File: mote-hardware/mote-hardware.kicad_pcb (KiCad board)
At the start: 2 copper layers, 93.6 x 102.8 mm, 67 parts, among them J1 USB_C_Receptacle_USB2.0_14P, J2 JST_XH2.54-SP, J4 SM03B-SRSS-TB, J5 Conn_01x03_Pin, J6 Conn_01x03_Pin, J7 JST_PH_B6B, J8 JST_PH_B6B, SW1 SW_Push, SW2 SW_Push, U1 RP2354_60QFN, U2 NCP1117-3.3_SOT223, U4 RP Radio Module 2, U5 DRV8833PW, U9 LSM6DS3, Y1 ABM8-272-T3

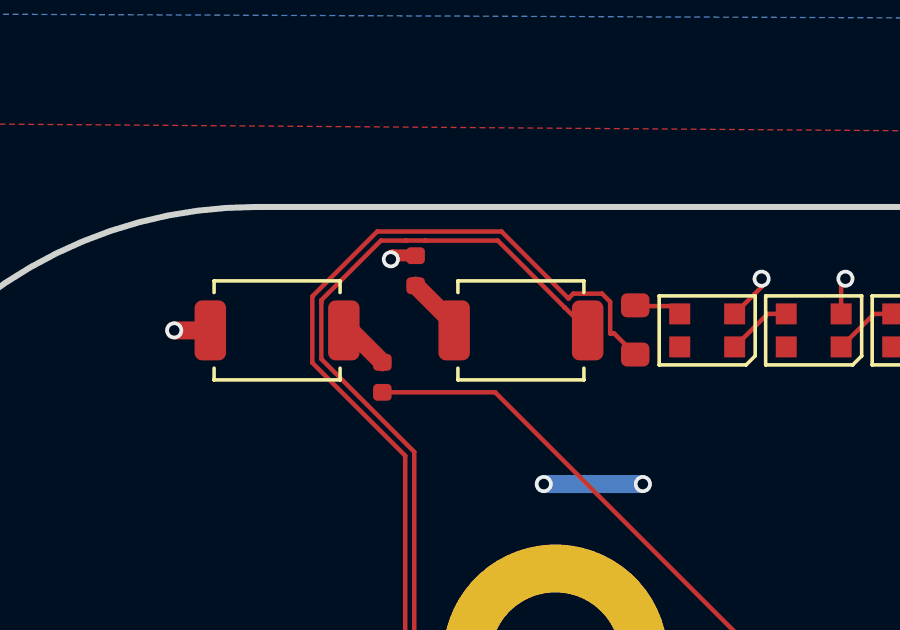
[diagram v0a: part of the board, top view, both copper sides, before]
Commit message: Add 3d models
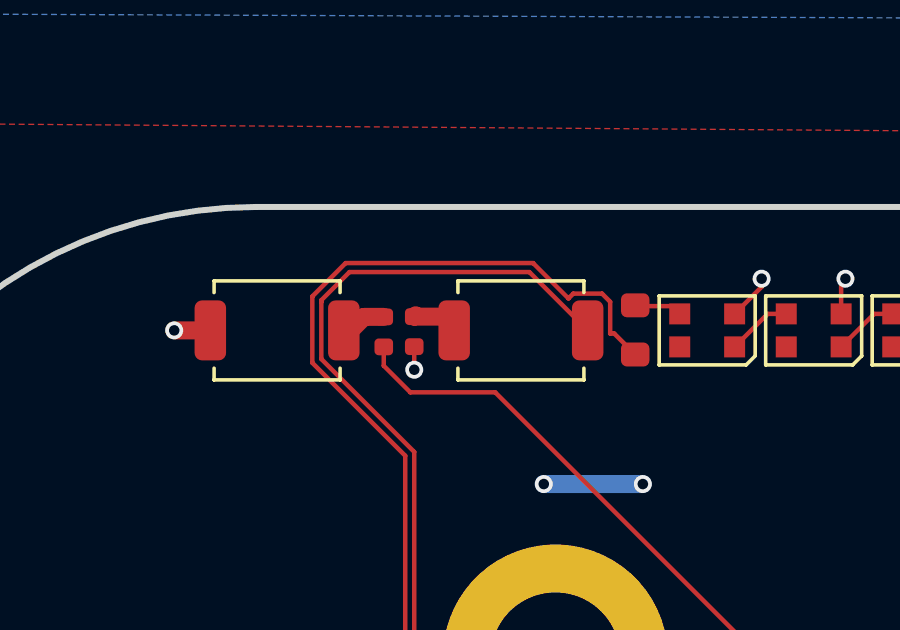
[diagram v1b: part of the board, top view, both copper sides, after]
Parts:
- moved R4 2.03 mm to (72.9, 43.7), turned to -90 degrees
- moved R6 1.51 mm to (71.9, 43.7)
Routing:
- net /rp2354/QSPI_SS: track 57.2 -> 58.1 mm
- net /status_led_tx: track 140.1 -> 139.2 mm
- net /rp2354/RUN: track 132.2 -> 131.4 mm

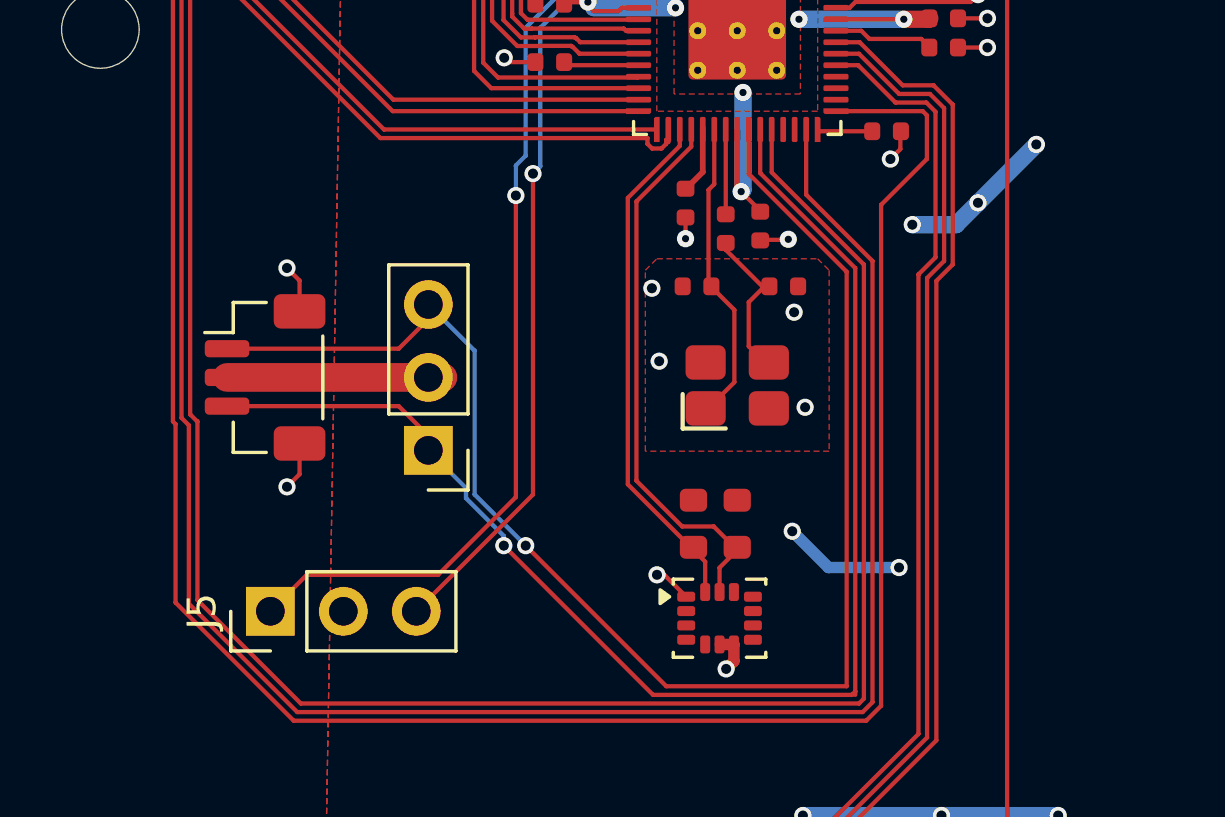
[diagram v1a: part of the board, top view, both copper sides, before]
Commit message: Add comments to schematic, respect ground pin on SWD and UART connectors
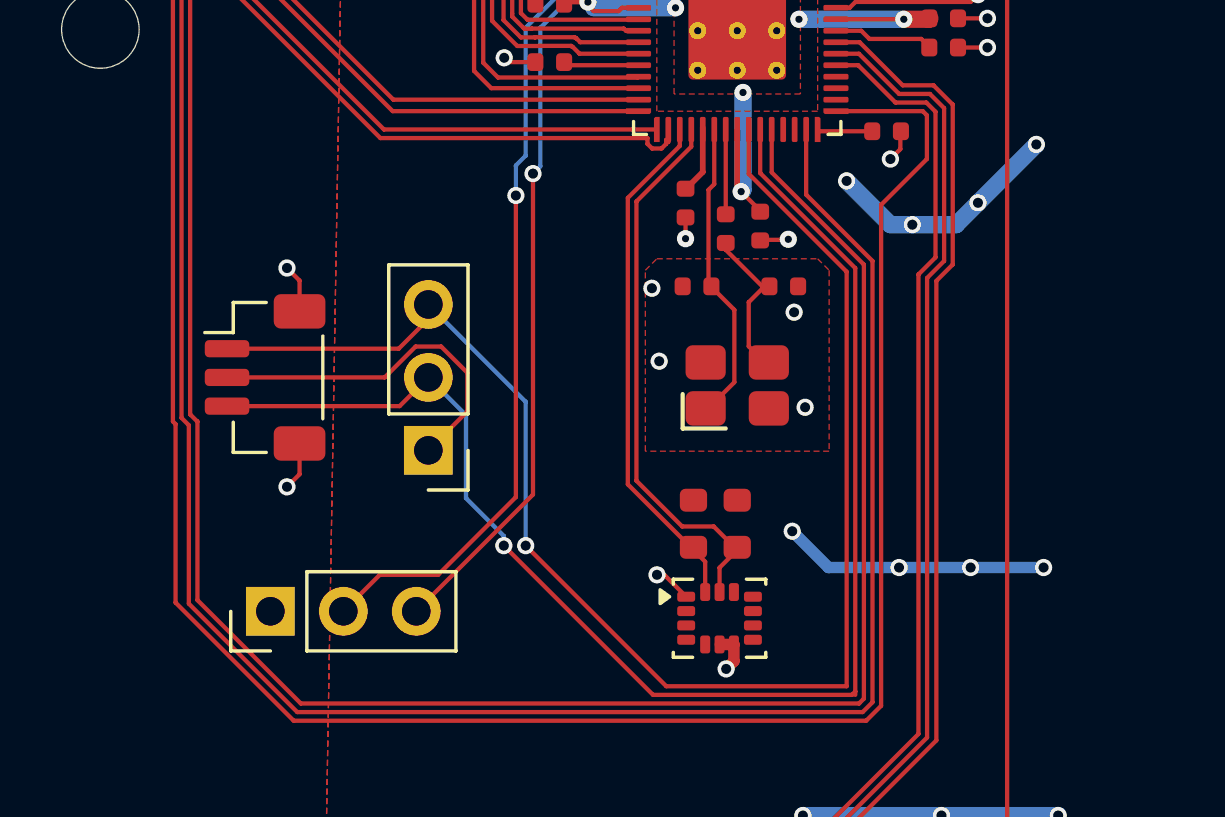
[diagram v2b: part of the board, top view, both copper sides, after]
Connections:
- J5 pad 1: /rp2354/UART0_TX -> GND
- J5 pad 2: GND -> /rp2354/UART0_TX
- J6 pad 1: /rp2354/SWD -> GND
- J6 pad 2: GND -> /rp2354/SWD
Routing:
- net /+3v3: track 67.2 -> 75.2 mm, vias 11 -> 14
- net GND: track 77.9 -> 82.9 mm
- net /rp2354/UART0_TX: track 32.0 -> 29.4 mm
- net /rp2354/SWD: track 48.1 -> 49.9 mm
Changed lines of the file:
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@@
 			(layers "*.Cu" "*.Mask")
 			(remove_unused_layers no)
-			(net 26 "/rp2354/SWD")
+			(net 1 "GND")
 			(pinfunction "Pin_1")
 			(pintype "passive")
@@
 			(layers "*.Cu" "*.Mask")
 			(remove_unused_layers no)
-			(net 1 "GND")
+			(net 26 "/rp2354/SWD")
 			(pinfunction "Pin_2")
 			(pintype "passive")
@@
 		)
 		(property "Value" "10u"
-			(at 0 1.68 0)
+			(at 0.254 -1.778 0)
 			(layer "F.Fab")
 			(effects
@@
 		)
 		(property "Value" "WS2812B-2020"
-			(at 0 2.2 0)
+			(at -2.935 2.752 0)
 			(layer "F.Fab")
 			(effects
@@
 		)
 		(property "Value" "WS2812B-2020"
-			(at 0 2.2 0)
+			(at 4.165 2.752 0)
 			(layer "F.Fab")
 			(effects
@@
 		)
 		(property "Value" "WS2812B-2020"
-			(at 0 2.2 0)
+			(at 0.615 2.752 0)
 			(layer "F.Fab")
 			(effects
@@
 		(property "Reference" "J5"
 			(at 0 -2.38 90)
-			(layer "F.SilkS")
+			(layer "Dwgs.User")
 			(effects
 				(font
@@
 			(layers "*.Cu" "*.Mask")
 			(remove_unused_layers no)
-			(net 70 "/rp2354/UART0_TX")
+			(net 1 "GND")
 			(pinfunction "Pin_1")
 			(pintype "passive")
@@
 			(layers "*.Cu" "*.Mask")
 			(remove_unused_layers no)
-			(net 1 "GND")
+			(net 70 "/rp2354/UART0_TX")
 			(pinfunction "Pin_2")
 			(pintype "passive")
@@
 	)
 	(segment
-		(start 83.582 72.1021)
-		(end 83.582001 72.102099)
-		(width 0.4)
+		(start 90.678 104.97672)
+		(end 90.678 106.323)
+		(width 0.15)
 		(layer "F.Cu")
 		(net 1)
 	)
 	(segment
-		(start 82.311 105.14)
-		(end 89.829 105.14)
-		(width 1)
+		(start 83.582 72.1021)
+		(end 83.582001 72.102099)
+		(width 0.4)
 		(layer "F.Cu")
 		(net 1)
@@
 	)
 	(segment
+		(start 87.80072 105.14)
+		(end 88.87572 104.065)
+		(width 0.15)
+		(layer "F.Cu")
+		(net 1)
+	)
+	(segment
 		(start 98.298 112.776)
 		(end 97.536 112.014)
@@
 	)
 	(segment
+		(start 82.311 105.14)
+		(end 87.80072 105.14)
+		(width 0.15)
+		(layer "F.Cu")
+		(net 1)
+	)
+	(segment
 		(start 87.128 43.096)
 		(end 87.128 42.066)
@@
 	)
 	(segment
+		(start 89.76628 104.065)
+		(end 90.678 104.97672)
+		(width 0.15)
+		(layer "F.Cu")
+		(net 1)
+	)
+	(segment
 		(start 84.598 76.496)
 		(end 84.556 76.454)
@@
 	)
 	(segment
+		(start 90.678 106.323)
+		(end 89.321 107.68)
+		(width 0.15)
+		(layer "F.Cu")
+		(net 1)
+	)
+	(segment
 		(start 83.578 43.096)
 		(end 84.477 42.197)
@@
 	)
 	(segment
+		(start 88.87572 104.065)
+		(end 89.76628 104.065)
+		(width 0.15)
+		(layer "F.Cu")
+		(net 1)
+	)
+	(segment
 		(start 113.552 51.322)
 		(end 113.538 51.308)
@@
 	)
 	(via
+		(at 108.204 111.76)
+		(size 0.6)
+		(drill 0.35)
+		(layers "F.Cu" "B.Cu")
+		(net 10)
+	)
+	(via
 		(at 101.991029 110.496075)
 		(size 0.6)
@@
 	)
 	(via
+		(at 103.886 98.298)
+		(size 0.6)
+		(drill 0.35)
+		(layers "F.Cu" "B.Cu")
+		(net 10)
+	)
+	(via
 		(at 94.996 88.392)
 		(size 0.6)
@@
 	)
 	(via
+		(at 110.744 111.76)
+		(size 0.6)
+		(drill 0.35)
+		(layers "F.Cu" "B.Cu")
+		(net 10)
+	)
+	(via
 		(at 111.252 120.396)
 		(size 0.6)
@@
 	)
 	(segment
+		(start 108.204 111.76)
+		(end 110.744 111.76)
+		(width 0.4)
+		(layer "B.Cu")
+		(net 10)
+	)
+	(segment
 		(start 107.188 120.396)
 		(end 111.252 120.396)
@@
 	)
 	(segment
+		(start 105.41 99.822)
+		(end 103.886 98.298)
+		(width 0.6)
+		(layer "B.Cu")
+		(net 10)
+	)
+	(segment
 		(start 88.138 68.7945)
 		(end 88.234 68.8905)
@@
 	)
 	(segment
+		(start 105.711 111.76)
+		(end 108.204 111.76)
+		(width 0.4)
+		(layer "B.Cu")
+		(net 10)
+	)
+	(segment
 		(start 102.362 120.396)
 		(end 107.188 120.396)
@@
 	)
 	(segment
+		(start 106.172 99.822)
+		(end 105.41 99.822)
+		(width 0.6)
+		(layer "B.Cu")
+		(net 10)
+	)
+	(segment
 		(start 101.276 89.134)
 		(end 101.08 88.938)
@@
 	(segment
 		(start 92.71 110.998)
-		(end 90.932 109.22)
+		(end 92.71 105.989)
 		(width 0.15)
 		(layer "B.Cu")
@@
 	)
 	(segment
-		(start 90.932 109.22)
-		(end 90.932 104.211)
-		(width 0.15)
-		(layer "B.Cu")
-		(net 25)
-	)
-	(segment
-		(start 90.932 104.211)
+		(start 92.71 105.989)
 		(end 89.321 102.6)
 		(width 0.15)
@@
 	)
 	(segment
-		(start 88.289 106.14)
-		(end 89.829 107.68)
-		(width 0.15)
-		(layer "F.Cu")
-		(net 26)
-	)
-	(segment
 		(start 82.311 106.14)
-		(end 88.289 106.14)
+		(end 88.321 106.14)
 		(width 0.15)
 		(layer "F.Cu")
@@
 	)
 	(segment
+		(start 88.321 106.14)
+		(end 89.321 105.14)
+		(width 0.15)
+		(layer "F.Cu")
+		(net 26)
+	)
+	(segment
 		(start 104.186 116.078)
 		(end 104.186 116.194)
@@
 	)
 	(segment
-		(start 90.632 108.991)
-		(end 89.321 107.68)
+		(start 90.632 109.344264)
+		(end 90.632 106.451)
 		(width 0.15)
 		(layer "B.Cu")
@@
 	)
 	(segment
-		(start 91.948 110.998)
-		(end 91.948 110.660264)
+		(start 90.632 106.451)
+		(end 89.321 105.14)
 		(width 0.15)
 		(layer "B.Cu")
@@
 	)
 	(segment
-		(start 90.632 109.344264)
-		(end 90.632 108.991)
+		(start 91.948 110.660264)
+		(end 90.632 109.344264)
 		(width 0.15)
 		(layer "B.Cu")
@@
 	)
 	(segment
-		(start 91.948 110.660264)
-		(end 90.632 109.344264)
+		(start 91.948 110.998)
+		(end 91.948 110.660264)
 		(width 0.15)
 		(layer "B.Cu")
@@
 	)
 	(segment
-		(start 85.09 112.014)
-		(end 89.662 112.014)
+		(start 89.662 112.014)
+		(end 87.63 112.014)
 		(width 0.15)
 		(layer "F.Cu")
@@
 	)
 	(segment
-		(start 89.662 112.014)
-		(end 92.367997 109.308003)
+		(start 87.63 112.014)
+		(end 86.36 113.284)
 		(width 0.15)
 		(layer "F.Cu")
@@
 	)
 	(segment
-		(start 83.82 113.284)
-		(end 85.09 112.014)
+		(start 89.662 112.014)
+		(end 92.367997 109.308003)
 		(width 0.15)
 		(layer "F.Cu")

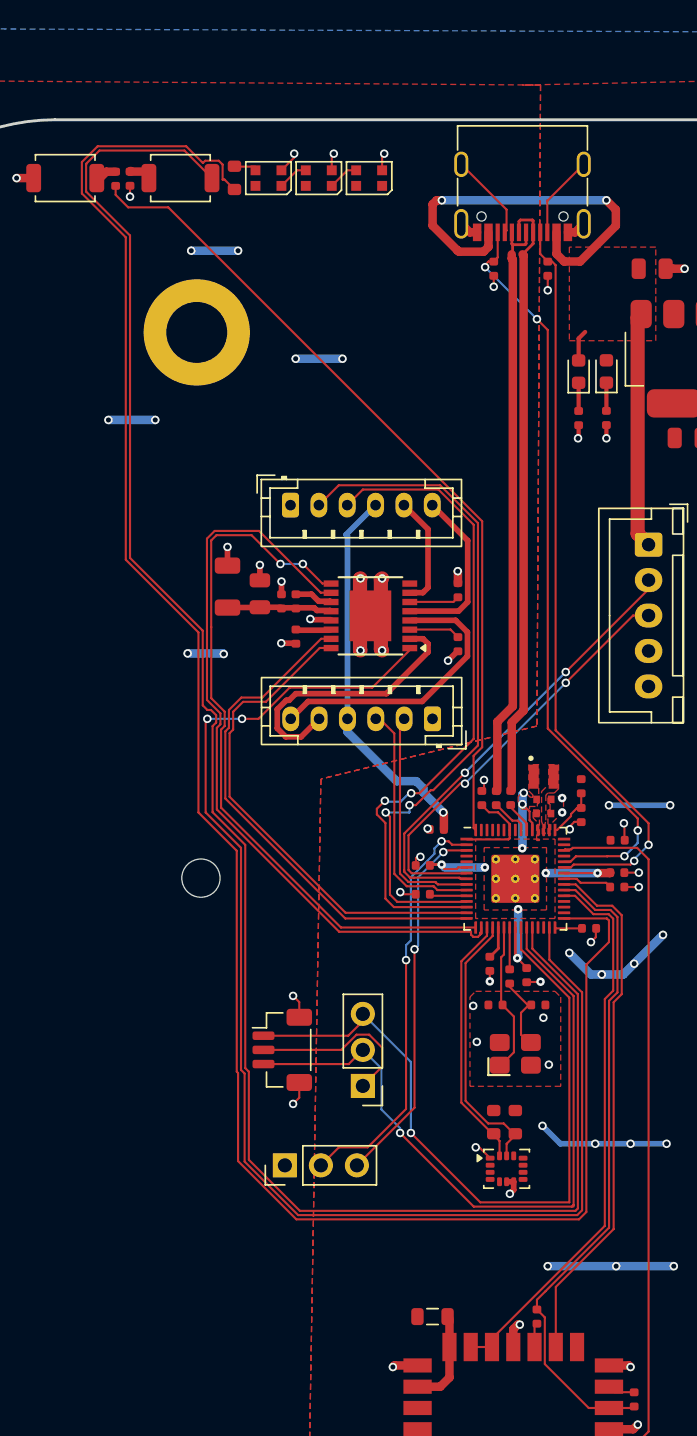
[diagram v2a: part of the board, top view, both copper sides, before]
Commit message: reformated a couple traces
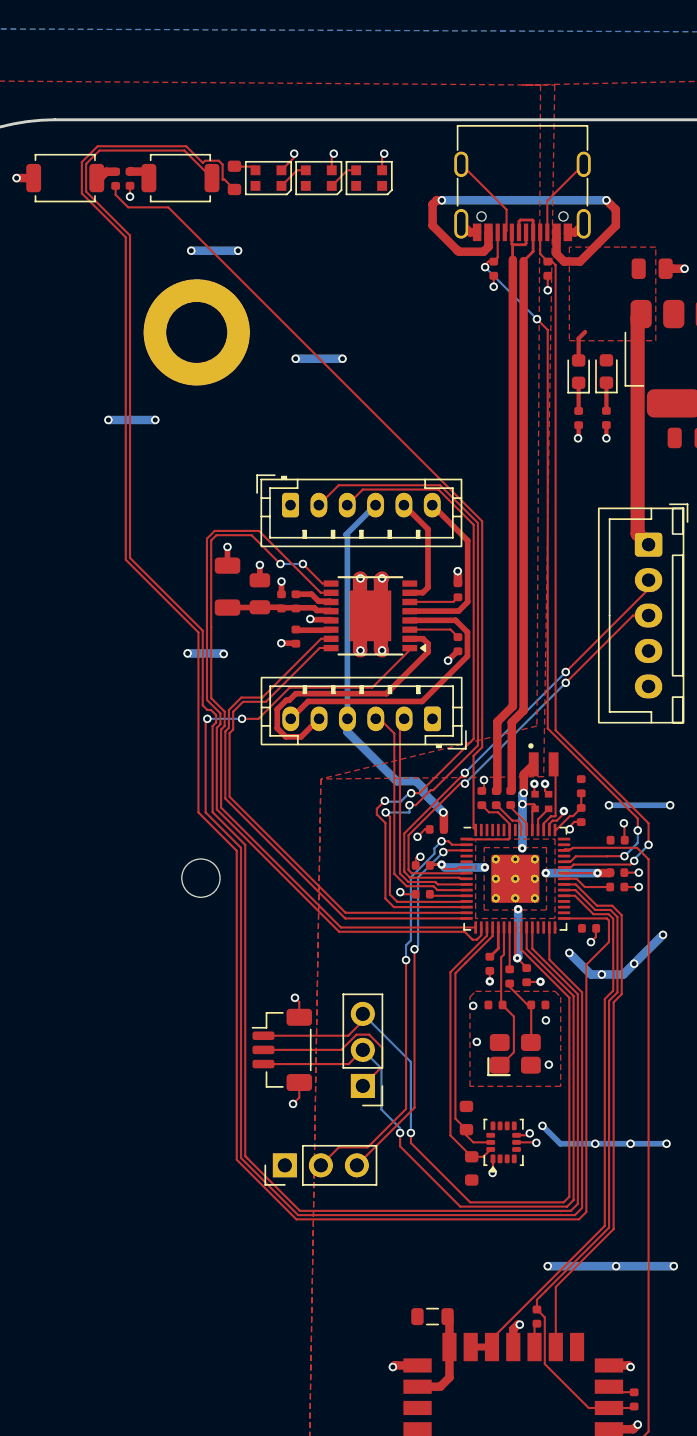
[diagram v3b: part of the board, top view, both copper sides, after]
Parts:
- moved R14 3.61 mm to (97.0, 113.5), turned to 90 degrees
- moved R15 3.46 mm to (96.6, 109.9)
- moved U9 1.88 mm to (99.2, 111.7), turned to 90 degrees
- moved C6 0.91 mm to (102.4, 87.6), turned to 90 degrees
- moved L1 0.87 mm to (102.1, 85.0)
- moved C7 0.64 mm to (101.5, 87.6), turned to 90 degrees
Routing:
- net /rp2354/VREG_LX: track 0.00 -> 5.52 mm
- net GND: track 82.9 -> 87.7 mm, vias 50 -> 52
- net /rp2354/+1v1: track 26.0 -> 28.9 mm
- net /imu_sda: track 18.0 -> 19.4 mm
- net /imu_scl: track 19.3 -> 18.2 mm
- removed copper zone on F.Cu, net (none)
- removed copper zone on F.Cu, net /rp2354/VREG_LX
